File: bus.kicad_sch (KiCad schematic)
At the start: 9 parts, among them J101 +60V IN

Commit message: Schematic complete: all sheets wired, ERC clean, netlist verified, cap ratings set
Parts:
- C101, C102, C103, C104, C105, C106: Voltage (none) -> 100V
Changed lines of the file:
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@@
+			)
+		)
+		(property "Voltage" "100V"
+			(at 88.9 87.63 0)
+			(hide yes)
+			(show_name no)
+			(do_not_autoplace no)
+			(effects
+				(font
+					(size 1.27 1.27)
+				)
 			)
 		)
@@
 			)
 		)
+		(property "Voltage" "100V"
+			(at 152.4 87.63 0)
+			(hide yes)
+			(show_name no)
+			(do_not_autoplace no)
+			(effects
+				(font
+					(size 1.27 1.27)
+				)
+			)
+		)
 		(pin "2"
 		)
@@
 			)
 		)
+		(property "Voltage" "100V"
+			(at 114.3 87.63 0)
+			(hide yes)
+			(show_name no)
+			(do_not_autoplace no)
+			(effects
+				(font
+					(size 1.27 1.27)
+				)
+			)
+		)
 		(pin "2"
 		)
@@
 			)
 		)
+		(property "Voltage" "100V"
+			(at 139.7 87.63 0)
+			(hide yes)
+			(show_name no)
+			(do_not_autoplace no)
+			(effects
+				(font
+					(size 1.27 1.27)
+				)
+			)
+		)
 		(pin "2"
 		)
@@
 			)
 		)
+		(property "Voltage" "100V"
+			(at 101.6 87.63 0)
+			(hide yes)
+			(show_name no)
+			(do_not_autoplace no)
+			(effects
+				(font
+					(size 1.27 1.27)
+				)
+			)
+		)
 		(pin "2"
 		)
@@
 			(at 127 87.63 0)
 			(hide yes)
+			(show_name no)
+			(do_not_autoplace no)
+			(effects
+				(font
+					(size 1.27 1.27)
+				)
+			)
+		)
+		(property "Voltage" "100V"
+			(at 127 87.63 0)
+			(hide yes)

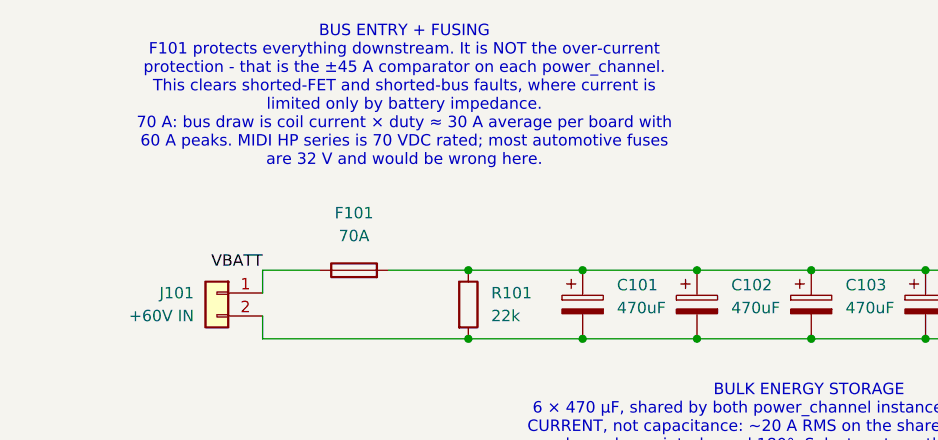
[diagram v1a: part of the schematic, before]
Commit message: All footprints assigned; fuse moved to harness; project footprint library added
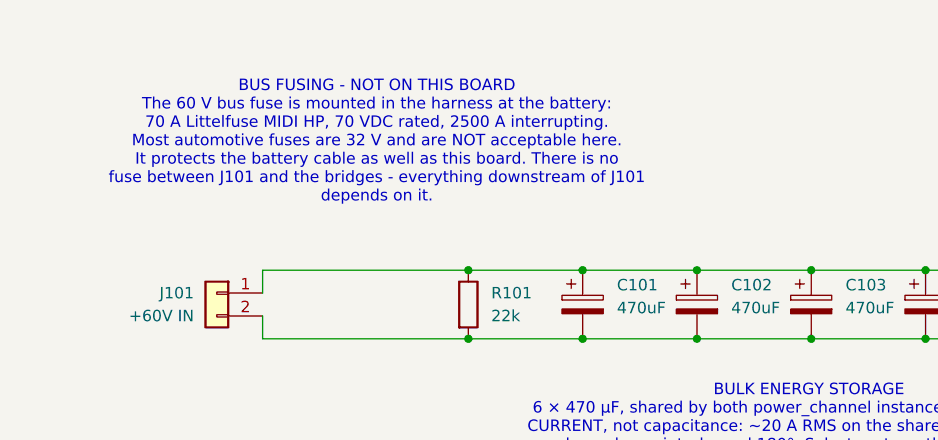
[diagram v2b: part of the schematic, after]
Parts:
- removed F101: 70A, symbol Device:Fuse
- J101: footprint (none) -> lev_lib:389690002; MPN Molex 38969-0002 -> 38969-0002
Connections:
- net VBATT is gone; now on net +60V: J101.1 (Pin_1)
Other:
- note added: "BUS FUSING - NOT ON THIS BOARD The 60 V bus fuse is mounted in the harness at the battery: 70 A Littelfuse MIDI HP, 70 VDC rated, 2500 A interrupting. Most automotive fuses are 32 V and are NOT acceptable here. It protects the battery cable as well as this board. There is no fuse between J101 and the bridges - everything downstream of J101 depends on it."
- note removed: "BUS ENTRY + FUSING F101 protects everything downstream. It is NOT the over-current protection - that is the ±45 A comparator on each power_channel. This clears shorted-FET and shorted-bus faults, where current is limited only by battery impedance. 70 A: bus draw is coil current × duty ≈ 30 A average per board with 60 A peaks. MIDI HP series is 70 VDC rated; most automotive fuses are 32 V and woul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"
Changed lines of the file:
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@@
 		(comment 2 "Shared by both power_channel instances.")
 	)
-	(text "BUS ENTRY + FUSING\nF101 protects everything downstream. It is NOT the over-current\nprotection - that is the ±45 A comparator on each power_channel.\nThis clears shorted-FET and shorted-bus faults, where current is\nlimited only by battery impedance.\n70 A: bus draw is coil current × duty ≈ 30 A average per board with\n60 A peaks. MIDI HP series is 70 VDC rated; most automotive fuses\nare 32 V and would be wrong here."
+	(text "BUS FUSING - NOT ON THIS BOARD\nThe 60 V bus fuse is mounted in the harness at the battery:\n70 A Littelfuse MIDI HP, 70 VDC rated, 2500 A interrupting.\nMost automotive fuses are 32 V and are NOT acceptable here.\nIt protects the battery cable as well as this board. There is no\nfuse between J101 and the bridges - everything downstream of J101\ndepends on it."
 		(exclude_from_sim no)
-		(at 69.088 64.516 0)
+		(at 66.04 69.596 0)
 		(effects
 			(font
@@
 	(wire
 		(pts
-			(xy 67.31 83.82) (xy 76.2 83.82)
-		)
-		(stroke
-			(width 0)
-			(type default)
-		)
-	)
-	(wire
-		(pts
 			(xy 152.4 91.44) (xy 160.02 91.44)
 		)
@@
 	(wire
 		(pts
-			(xy 53.34 83.82) (xy 59.69 83.82)
+			(xy 53.34 83.82) (xy 76.2 83.82)
 		)
 		(stroke
@@
 			(width 0)
 			(type default)
-		)
-	)
-	(label "VBATT"
-		(at 53.34 83.82 180)
-		(effects
-			(font
-				(size 1.27 1.27)
-			)
-			(justify right bottom)
 		)
 	)
@@
 			)
 		)
-		(property "Footprint" ""
+		(property "Footprint" "lev_lib:389690002"
 			(at 48.26 86.36 0)
 			(hide yes)
@@
 			)
 		)
-		(property "MPN" "Molex 38969-0002"
+		(property "MPN" "38969-0002"
 			(at 48.26 86.36 0)
 			(hide yes)
@@
 					(unit 1)
 				)
-			)
-		)
-	)
-	(symbol
-		(lib_id "Device:Fuse")
-		(at 63.5 83.82 90)
-		(unit 1)
-		(body_style 1)
-		(exclude_from_sim no)
-		(in_bom yes)
-		(on_board yes)
-		(in_pos_files yes)
-		(dnp no)
-		(fields_autoplaced yes)
-		(property "Reference" "F101"
-			(at 63.5 77.47 90)
-			(show_name no)
-			(do_not_autoplace no)
-			(effects
-				(font
-					(size 1.27 1.27)
-				)
-			)
-		)
-		(property "Value" "70A"
-			(at 63.5 80.01 90)
-			(show_name no)
-			(do_not_autoplace no)
-			(effects
-				(font
-					(size 1.27 1.27)
-				)
-			)
-		)
-		(property "Footprint" ""
-			(at 63.5 85.598 90)
-			(hide yes)
-			(show_name no)
-			(do_not_autoplace no)
-			(effects
-				(font
-					(size 1.27 1.27)
-				)
-			)
-		)
-		(property "Datasheet" ""
-			(at 63.5 83.82 0)
-			(hide yes)
-			(show_name no)
-			(do_not_autoplace no)
-			(effects
-				(font
-					(size 1.27 1.27)
-				)
-			)
-		)
-		(property "Description" "Fuse"
-			(at 63.5 83.82 0)
-			(hide yes)
-			(show_name no)
-			(do_not_autoplace no)
-			(effects
-				(font
-					(size 1.27 1.27)
-				)
-			)
-		)
-		(pin "1"
-		)
-		(pin "2"
-		)
-		(instances
-			(project "final_lev"
-				(path "/0a40c0f2-6b4c-4590-a920-c8cc820982d1/ad4a7ac2-7247-48cc-af34-a682db78e613"
-					(reference "F101")
-					(unit 1)
-				)

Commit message: Adversarial review fixes: set-dominant latch, MCU enable, 3V3 hold-up, sense chain, 16-way connector
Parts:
- C101, C102, C103, C104, C105, C106: footprint Capacitor_THT:CP_Radial_D18.0mm_P7.50mm -> Capacitor_THT:CP_Radial_D16.0mm_P7.50mm; MPN (none) -> 100ZLH470MEFC16X31.5
- R101: footprint Resistor_SMD:R_1206_3216Metric_Pad1.30x1.75mm_HandSolder -> Resistor_SMD:R_2512_6332Metric; Power (none) -> 1W
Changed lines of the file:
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@@
 			)
 		)
-		(property "Footprint" "Capacitor_THT:CP_Radial_D18.0mm_P7.50mm"
+		(property "Footprint" "Capacitor_THT:CP_Radial_D16.0mm_P7.50mm"
 			(at 89.8652 91.44 0)
 			(hide yes)
@@
 		)
 		(property "Voltage" "100V"
+			(at 88.9 87.63 0)
+			(hide yes)
+			(show_name no)
+			(do_not_autoplace no)
+			(effects
+				(font
+					(size 1.27 1.27)
+				)
+			)
+		)
+		(property "MPN" "100ZLH470MEFC16X31.5"
 			(at 88.9 87.63 0)
 			(hide yes)
@@
 			)
 		)
-		(property "Footprint" "Capacitor_THT:CP_Radial_D18.0mm_P7.50mm"
+		(property "Footprint" "Capacitor_THT:CP_Radial_D16.0mm_P7.50mm"
 			(at 153.3652 91.44 0)
 			(hide yes)
@@
 		)
 		(property "Voltage" "100V"
+			(at 152.4 87.63 0)
+			(hide yes)
+			(show_name no)
+			(do_not_autoplace no)
+			(effects
+				(font
+					(size 1.27 1.27)
+				)
+			)
+		)
+		(property "MPN" "100ZLH470MEFC16X31.5"
 			(at 152.4 87.63 0)
 			(hide yes)
@@
 			)
 		)
-		(property "Footprint" "Resistor_SMD:R_1206_3216Metric_Pad1.30x1.75mm_HandSolder"
+		(property "Footprint" "Resistor_SMD:R_2512_6332Metric"
 			(at 74.422 87.63 90)
 			(hide yes)
@@
 		)
 		(property "Description" "Resistor"
+			(at 76.2 87.63 0)
+			(hide yes)
+			(show_name no)
+			(do_not_autoplace no)
+			(effects
+				(font
+					(size 1.27 1.27)
+				)
+			)
+		)
+		(property "Power" "1W"
 			(at 76.2 87.63 0)
 			(hide yes)
@@
 			)
 		)
-		(property "Footprint" "Capacitor_THT:CP_Radial_D18.0mm_P7.50mm"
+		(property "Footprint" "Capacitor_THT:CP_Radial_D16.0mm_P7.50mm"
 			(at 115.2652 91.44 0)
 			(hide yes)
@@
 		)
 		(property "Voltage" "100V"
+			(at 114.3 87.63 0)
+			(hide yes)
+			(show_name no)
+			(do_not_autoplace no)
+			(effects
+				(font
+					(size 1.27 1.27)
+				)
+			)
+		)
+		(property "MPN" "100ZLH470MEFC16X31.5"
 			(at 114.3 87.63 0)
 			(hide yes)
@@
 			)
 		)
-		(property "Footprint" "Capacitor_THT:CP_Radial_D18.0mm_P7.50mm"
+		(property "Footprint" "Capacitor_THT:CP_Radial_D16.0mm_P7.50mm"
 			(at 140.6652 91.44 0)
 			(hide yes)
@@
 		)
 		(property "Voltage" "100V"
+			(at 139.7 87.63 0)
+			(hide yes)
+			(show_name no)
+			(do_not_autoplace no)
+			(effects
+				(font
+					(size 1.27 1.27)
+				)
+			)
+		)
+		(property "MPN" "100ZLH470MEFC16X31.5"
 			(at 139.7 87.63 0)
 			(hide yes)
@@
 			)
 		)
-		(property "Footprint" "Capacitor_THT:CP_Radial_D18.0mm_P7.50mm"
+		(property "Footprint" "Capacitor_THT:CP_Radial_D16.0mm_P7.50mm"
 			(at 102.5652 91.44 0)
 			(hide yes)
@@
 		)
 		(property "Voltage" "100V"
+			(at 101.6 87.63 0)
+			(hide yes)
+			(show_name no)
+			(do_not_autoplace no)
+			(effects
+				(font
+					(size 1.27 1.27)
+				)
+			)
+		)
+		(property "MPN" "100ZLH470MEFC16X31.5"
 			(at 101.6 87.63 0)
 			(hide yes)
@@
 			)
 		)
-		(property "Footprint" "Capacitor_THT:CP_Radial_D18.0mm_P7.50mm"
+		(property "Footprint" "Capacitor_THT:CP_Radial_D16.0mm_P7.50mm"
 			(at 127.9652 91.44 0)
 			(hide yes)
@@
 			(at 127 87.63 0)
 			(hide yes)
+			(show_name no)
+			(do_not_autoplace no)
+			(effects
+				(font
+					(size 1.27 1.27)
+				)
+			)
+		)
+		(property "MPN" "100ZLH470MEFC16X31.5"
+			(at 127 87.63 0)
+			(hide yes)

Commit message: Coil pours, test points, and a pad-rotation defect found by tooling
Board:

- 13 test points placed, grounds first so every signal point sits within 7.5 mm of its own ground return

- All four 30 A coil pours drawn on B.Cu, single polygons, 10.7-11.0 mm at the narrowest cut

- 34 vias transitioning the two A legs from the surface-mount shunts down to B.Cu, 15 at 2.0 A on CH1 and 19 at 1.58 A on CH2

- The B legs need no vias: every pad carrying their current is through-hole

Fixed:

- 20 footprints had pads that did not follow their body rotation, 5 of them off by 90 degrees, which turns a 1.175 x 1.450 mm pad across the part instead of along it. Repaired by Update Footprints from Library

- A12 corrected twice. The mounting holes are plated M3 pads on all four layers with no net, not the unplated holes I first reported

Tools:

- pour_check.py rasterises pour outlines at 0.05 mm; lay.py's bounding-box zone check was blind to polygons and missed a 6.5 mm band that needed 10.7

- lay.py gained pad-rotation and zone-priority checks, both regression tested against the broken versions
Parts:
- added TP213: TestPoint, TestPoint:TestPoint_Loop_D2.50mm_Drill1.0mm, symbol Connector:TestPoint
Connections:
- net GND: now also TP213.1
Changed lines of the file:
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@@
+	)
+	(symbol
+		(lib_id "Connector:TestPoint")
+		(at 63.5 127 0)
+		(unit 1)
+		(body_style 1)
+		(exclude_from_sim no)
+		(in_bom yes)
+		(on_board yes)
+		(in_pos_files yes)
+		(dnp no)
+		(fields_autoplaced yes)
+		(property "Reference" "TP213"
+			(at 66.04 122.4279 0)
+			(show_name no)
+			(do_not_autoplace no)
+			(effects
+				(font
+					(size 1.27 1.27)
+				)
+				(justify left)
+			)
+		)
+		(property "Value" "TestPoint"
+			(at 66.04 124.9679 0)
+			(show_name no)
+			(do_not_autoplace no)
+			(effects
+				(font
+					(size 1.27 1.27)
+				)
+				(justify left)
+			)
+		)
+		(property "Footprint" "TestPoint:TestPoint_Loop_D2.50mm_Drill1.0mm"
+			(at 68.58 127 0)
+			(hide yes)
+			(show_name no)
+			(do_not_autoplace no)
+			(effects
+				(font
+					(size 1.27 1.27)
+				)
+			)
+		)
+		(property "Datasheet" ""
+			(at 68.58 127 0)
+			(hide yes)
+			(show_name no)
+			(do_not_autoplace no)
+			(effects
+				(font
+					(size 1.27 1.27)
+				)
+			)
+		)
+		(property "Description" "test point"
+			(at 63.5 127 0)
+			(hide yes)
+			(show_name no)
+			(do_not_autoplace no)
+			(effects
+				(font
+					(size 1.27 1.27)
+				)
+			)
+		)
+		(pin "1"
+		)
+		(instances
+			(project "final_lev"
+				(path "/0a40c0f2-6b4c-4590-a920-c8cc820982d1/ad4a7ac2-7247-48cc-af34-a682db78e613"
+					(reference "TP213")
+					(unit 1)
+				)
+			)
+		)
 	)
 	(symbol
@@
 					(unit 1)
 				)
+			)
+		)
+	)
+	(symbol
+		(lib_id "power:GND")
+		(at 63.5 127 0)
+		(unit 1)
+		(body_style 1)
+		(exclude_from_sim no)
+		(in_bom yes)
+		(on_board yes)
+		(in_pos_files yes)
+		(dnp no)
+		(fields_autoplaced yes)
+		(property "Reference" "#PWR0249"
+			(at 63.5 133.35 0)
+			(hide yes)
+			(show_name no)
+			(do_not_autoplace no)
+			(effects
+				(font
+					(size 1.27 1.27)
+				)
+			)
+		)
+		(property "Value" "GND"
+			(at 63.5 132.08 0)
+			(show_name no)
+			(do_not_autoplace no)
+			(effects
+				(font
+					(size 1.27 1.27)
+				)
+			)
+		)
+		(property "Footprint" ""
+			(at 63.5 127 0)
+			(hide yes)
+			(show_name no)
+			(do_not_autoplace no)
+			(effects
+				(font
+					(size 1.27 1.27)
+				)
+			)
+		)
+		(property "Datasheet" ""
+			(at 63.5 127 0)
+			(hide yes)
+			(show_name no)
+			(do_not_autoplace no)
+			(effects
+				(font
+					(size 1.27 1.27)
+				)
+			)
+		)
+		(property "Description" "Power symbol creates a global label with name \"GND\" , ground"
+			(at 63.5 127 0)
+			(hide yes)
+			(show_name no)
+			(do_not_autoplace no)
+			(effects
+				(font
+					(size 1.27 1.27)
+				)
+			)
+		)
+		(pin "1"
+		)
+		(instances
+			(project "final_lev"
+				(path "/0a40c0f2-6b4c-4590-a920-c8cc820982d1/ad4a7ac2-7247-48cc-af34-a682db78e613"
+					(reference "#PWR0249")
+					(unit 1)
+				)
